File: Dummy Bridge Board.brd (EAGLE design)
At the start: 86.4 x 113.7 mm, 102 parts, among them J2 5787834-1, U14 ADUM3160BRWZ-RL, U21 CD4050BD, U22 PDS1-S5-S5-M-TR, U28 FT4232HL, U29 SN74HC595DR, U30 LP5907MFX-3.3/NOPB, U49 TL7712A-SOIC, U9 TPS54540DDARQ1, Y2 CX3225GB12000P0HPQCC

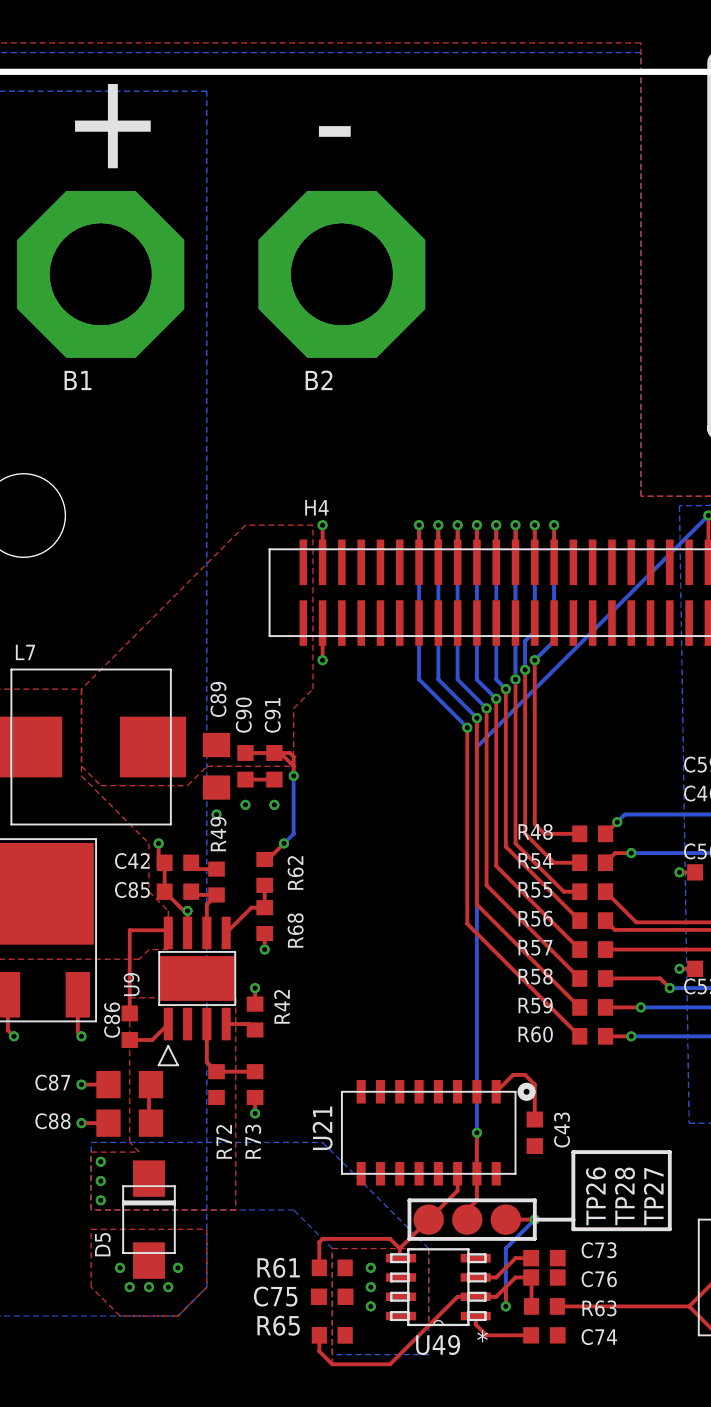
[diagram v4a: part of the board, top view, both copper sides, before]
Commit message: Added +3V3 Buck and finished BOM- Ready to order
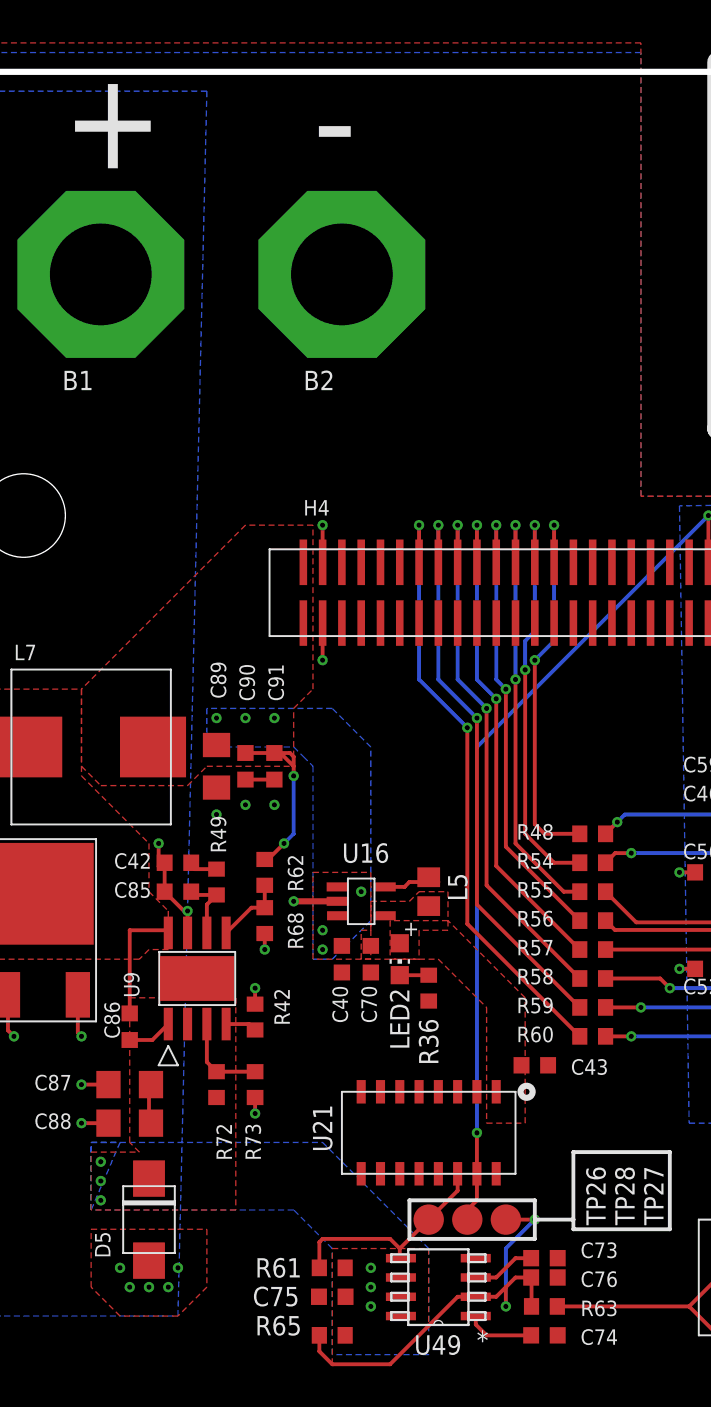
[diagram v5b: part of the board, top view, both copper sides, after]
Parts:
- added C40: 4.7uF, rcl:C0603K
- added C70: 10uF, rcl:C0603K
- added L5: 2.2uH, FormE:0805
- added LED2: GREEN, FormE:CHIP-LED0805
- added R36: 1k, rcl:R0603
- added U16: LM3671MF-3.3/NOPB, FormE:SOT23-5
- moved C43 4.45 mm to (38.1, 48.3), turned to 0 degrees
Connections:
- new net N$56: LED2.C, R36.2
- new net N$57: L5.1, U16.5
- net +3V3: now also C70.1, L5.2, LED2.A, U16.4
- net +5V: now also C40.1, U16.1, U16.3
- net GND: now also C40.2, C70.2, R36.1, U16.2
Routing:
- net +3V3: track 5.56 -> 0.00 mm
- net N$57: track 0.00 -> 4.11 mm
- net GND: track 92.3 -> 95.2 mm, vias 52 -> 53
- net N$56: track 0.00 -> 1.91 mm
- net +5V: vias 2 -> 8
- added copper zone on layer 1, net +3V3
- added copper zone on layer 16, net +5V
- added copper zone on layer 16, net N$1
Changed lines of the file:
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@@
 <element name="C89" library="rcl" package="C1206" value="47uF" x="17.145" y="67.945" smashed="yes" rot="R270">
 <attribute name="PARTNO" value="GRM31CR61A476ME15L" x="17.145" y="67.945" size="1.778" layer="27" rot="R270" display="off"/>
-<attribute name="NAME" x="17.78" y="71.12" size="1.016" layer="25" rot="R90"/>
+<attribute name="NAME" x="17.78" y="72.39" size="1.016" layer="25" rot="R90"/>
 <attribute name="VALUE" x="14.605" y="69.215" size="1.27" layer="27" rot="R270"/>
 </element>
 <element name="C90" library="rcl" package="C0603K" value="10uF" x="19.05" y="67.945" smashed="yes" rot="R270">
 <attribute name="PARTNO" value="GRM21BR61E106KA73L" x="19.05" y="67.945" size="1.778" layer="27" rot="R270" display="off"/>
-<attribute name="NAME" x="18.43" y="72.555" size="1.016" layer="25" rot="R270"/>
+<attribute name="NAME" x="19.67" y="72.225" size="1.016" layer="25" rot="R90"/>
 <attribute name="VALUE" x="17.4" y="68.745" size="1.016" layer="27" rot="R270"/>
 </element>
 <element name="C91" library="rcl" package="C0603K" value="10uF" x="20.955" y="67.945" smashed="yes" rot="R270">
 <attribute name="PARTNO" value="GRM21BR61E106KA73L" x="20.955" y="67.945" size="1.778" layer="27" rot="R270" display="off"/>
-<attribute name="NAME" x="20.335" y="72.555" size="1.016" layer="25" rot="R270"/>
+<attribute name="NAME" x="21.575" y="72.225" size="1.016" layer="25" rot="R90"/>
 <attribute name="VALUE" x="19.305" y="68.745" size="1.016" layer="27" rot="R270"/>
 </element>
@@
 <attribute name="NAME" x="24.765" y="42.545" size="1.27" layer="25" rot="R90"/>
 </element>
-<element name="C43" library="rcl" package="C0603K" value="0.1uF" x="38.1" y="43.815" smashed="yes" rot="R270">
-<attribute name="PARTNO" value="GRM21BR71E104KA01L" x="56.515" y="50.165" size="1.016" layer="27" rot="R270" display="off"/>
-<attribute name="NAME" x="39.385" y="45.25" size="1.016" layer="25" rot="R270"/>
-<attribute name="VALUE" x="36.45" y="44.615" size="1.016" layer="27" rot="R270"/>
+<element name="C43" library="rcl" package="C0603K" value="0.1uF" x="38.1" y="48.26" smashed="yes">
+<attribute name="PARTNO" value="GRM21BR71E104KA01L" x="31.75" y="66.675" size="1.016" layer="27" display="off"/>
+<attribute name="NAME" x="40.475" y="47.64" size="1.016" layer="25"/>
+<attribute name="VALUE" x="37.3" y="46.61" size="1.016" layer="27"/>
 </element>
 <element name="U49" library="FormE" package="D8" value="TL7712A-SOIC" x="31.75" y="33.655" smashed="yes" rot="R180">
@@
 <attribute name="PARTNO" value="FSM4JSMATR" x="60.96" y="85.09" size="1.016" layer="27" rot="R180" display="off"/>
 <attribute name="NAME" x="57.15" y="35.56" size="1.27" layer="25" rot="R270"/>
+</element>
+<element name="LED2" library="FormE" package="CHIP-LED0805" value="GREEN" x="29.21" y="55.245" smashed="yes" rot="R180">
+<attribute name="PARTNO" value="598-8170-107F" x="36.195" y="46.355" size="1.016" layer="27" rot="R180" display="off"/>
+<attribute name="NAME" x="28.575" y="53.34" size="1.27" layer="25" rot="R270"/>
+<attribute name="VALUE" x="26.67" y="56.515" size="1.27" layer="27" rot="R270"/>
+</element>
+<element name="R36" library="rcl" package="R0603" value="1k" x="31.115" y="53.34" smashed="yes" rot="R90">
+<attribute name="PARTNO" value="ERJ-6ENF1001V" x="22.86" y="40.64" size="1.016" layer="27" rot="R90" display="off"/>
+<attribute name="NAME" x="31.75" y="48.26" size="1.27" layer="25" rot="R90"/>
+<attribute name="VALUE" x="33.02" y="52.705" size="1.27" layer="27" rot="R90"/>
+</element>
+<element name="U16" library="FormE" package="SOT23-5" value="LM3671MF-3.3/NOPB" x="26.67" y="59.055" smashed="yes" rot="R270">
+<attribute name="PARTNO" value="LM3671MF-3.3/NOPB" x="34.925" y="72.39" size="1.016" layer="27" rot="R270" display="off"/>
+<attribute name="NAME" x="25.4" y="61.595" size="1.27" layer="25"/>
+</element>
+<element name="C40" library="rcl" package="C0603K" value="4.7uF" x="25.4" y="55.245" smashed="yes" rot="R270">
+<attribute name="PARTNO" value="GRM188R61A475KE15D" x="33.655" y="67.945" size="1.016" layer="27" rot="R270" display="off"/>
+<attribute name="NAME" x="24.78" y="53.505" size="1.016" layer="25" rot="R270"/>
+<attribute name="VALUE" x="23.75" y="56.045" size="1.016" layer="27" rot="R270"/>
+</element>
+<element name="C70" library="rcl" package="C0603K" value="10uF" x="27.305" y="55.245" smashed="yes" rot="R270">
+<attribute name="PARTNO" value="GRM21BR61E106KA73L" x="31.115" y="73.66" size="1.016" layer="27" rot="R270" display="off"/>
+<attribute name="NAME" x="26.685" y="53.505" size="1.016" layer="25" rot="R270"/>
+<attribute name="VALUE" x="25.655" y="56.045" size="1.016" layer="27" rot="R270"/>
+</element>
+<element name="L5" library="FormE" package="0805" value="2.2uH" x="31.115" y="59.69" smashed="yes" rot="R270">
+<attribute name="PARTNO" value="74479775222" x="17.145" y="78.74" size="1.016" layer="27" rot="R270" display="off"/>
+<attribute name="NAME" x="33.655" y="59.055" size="1.27" layer="25" rot="R90"/>
+<attribute name="VALUE" x="28.575" y="60.325" size="1.27" layer="27" rot="R270"/>
 </element>
 </elements>
@@
 <contactref element="S2" pad="3"/>
 <contactref element="C76" pad="2"/>
+<contactref element="R36" pad="1"/>
+<contactref element="U16" pad="2"/>
+<contactref element="C40" pad="2"/>
+<contactref element="C70" pad="2"/>
+<wire x1="25.12" y1="59.055" x2="22.225" y2="59.055" width="0.4064" layer="1"/>
+<via x="22.225" y="59.055" extent="1-16" drill="0.3302" diameter="0.254"/>
 </signal>
 <signal name="+5V">
@@
 <wire x1="22.225" y1="68.58" x2="21.985" y2="68.82" width="0.254" layer="1"/>
 <wire x1="21.985" y1="68.82" x2="20.955" y2="68.82" width="0.254" layer="1"/>
+<contactref element="U16" pad="3"/>
+<contactref element="U16" pad="1"/>
+<contactref element="C40" pad="1"/>
+<polygon width="0.254" layer="1" rank="2">
+<vertex x="27.305" y="60.96"/>
+<vertex x="27.305" y="55.245"/>
+<vertex x="23.495" y="55.245"/>
+<vertex x="23.495" y="60.96"/>
+</polygon>
+<via x="26.67" y="59.69" extent="1-16" drill="0.3302" diameter="0.254"/>
+<via x="24.13" y="57.15" extent="1-16" drill="0.3302" diameter="0.254"/>
+<via x="24.13" y="55.88" extent="1-16" drill="0.3302" diameter="0.254"/>
+<via x="17.145" y="71.12" extent="1-16" drill="0.3302" diameter="0.254"/>
+<via x="19.05" y="71.12" extent="1-16" drill="0.3302" diameter="0.254"/>
+<via x="20.955" y="71.12" extent="1-16" drill="0.3302" diameter="0.254"/>
+<polygon width="0.254" layer="16">
+<vertex x="17.145" y="69.215"/>
+<vertex x="22.225" y="69.215"/>
+<vertex x="22.86" y="68.58"/>
+<vertex x="23.495" y="67.945"/>
+<vertex x="23.495" y="55.245"/>
+<vertex x="24.765" y="55.245"/>
+<vertex x="27.305" y="57.785"/>
+<vertex x="27.305" y="67.945"/>
+<vertex x="27.305" y="69.215"/>
+<vertex x="24.765" y="71.755"/>
+<vertex x="16.51" y="71.755"/>
+<vertex x="16.51" y="69.215"/>
+</polygon>
 </signal>
 <signal name="VCC">
@@
 <vertex x="2.54" y="31.75"/>
 <vertex x="14.605" y="31.75"/>
-<vertex x="16.51" y="33.655"/>
 </polygon>
 <polygon width="0.254" layer="1">
@@
 <contactref element="U21" pad="1"/>
 <contactref element="C43" pad="1"/>
-<wire x1="35.56" y1="46.515" x2="36.67" y2="47.625" width="0.254" layer="1"/>
-<wire x1="36.67" y1="47.625" x2="37.465" y2="47.625" width="0.254" layer="1"/>
-<wire x1="37.465" y1="47.625" x2="38.1" y2="46.99" width="0.254" layer="1"/>
-<wire x1="38.1" y1="46.99" x2="38.1" y2="44.69" width="0.254" layer="1"/>
+<contactref element="C70" pad="1"/>
+<contactref element="U16" pad="4"/>
+<contactref element="L5" pad="2"/>
+<contactref element="LED2" pad="A"/>
+<polygon width="0.254" layer="1">
+<vertex x="26.67" y="55.245"/>
+<vertex x="26.67" y="57.15"/>
+<vertex x="27.305" y="57.15"/>
+<vertex x="27.305" y="59.055"/>
+<vertex x="29.845" y="59.055"/>
+<vertex x="30.48" y="59.69"/>
+<vertex x="32.385" y="59.69"/>
+<vertex x="32.385" y="57.15"/>
+<vertex x="30.48" y="57.15"/>
+<vertex x="30.48" y="55.245"/>
+</polygon>
+<polygon width="0.4064" layer="1">
+<vertex x="37.465" y="52.705"/>
+<vertex x="32.385" y="57.785"/>
+<vertex x="28.575" y="57.785"/>
+<vertex x="28.575" y="55.245"/>
+<vertex x="31.75" y="55.245"/>
+<vertex x="34.925" y="52.07"/>
+<vertex x="34.925" y="44.45"/>
+<vertex x="37.465" y="44.45"/>
+</polygon>
 </signal>
 <signal name="!POR">
@@
 <wire x1="50.455" y1="34.58" x2="50.455" y2="38.84" width="0.254" layer="1"/>
 </signal>
+<signal name="N$56">
+<contactref element="R36" pad="2"/>
+<contactref element="LED2" pad="C"/>
+<wire x1="29.21" y1="54.195" x2="29.215" y2="54.19" width="0.254" layer="1"/>
+<wire x1="29.215" y1="54.19" x2="31.115" y2="54.19" width="0.254" layer="1"/>
+</signal>
+<signal name="N$57">
+<contactref element="U16" pad="5"/>
+<contactref element="L5" pad="1"/>
+<wire x1="28.22" y1="60.005" x2="29.525" y2="60.005" width="0.254" layer="1"/>
+<wire x1="29.525" y1="60.005" x2="29.845" y2="60.325" width="0.254" layer="1"/>
+<wire x1="29.845" y1="60.325" x2="31.43" y2="60.325" width="0.254" layer="1"/>
+<wire x1="31.75" y1="60.325" x2="31.43" y2="60.325" width="0.254" layer="1"/>
+<wire x1="31.43" y1="60.325" x2="31.115" y2="60.64" width="0.254" layer="1"/>
+</signal>
+<signal name="N$1">
+<polygon width="0.254" layer="16">
+<vertex x="8.89" y="38.735"/>
+<vertex x="8.89" y="43.18"/>
+<vertex x="10.795" y="43.18"/>
+</polygon>
+</signal>
 </signals>
